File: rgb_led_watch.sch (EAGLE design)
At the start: 30 parts, among them IC4 74V1T126CTR

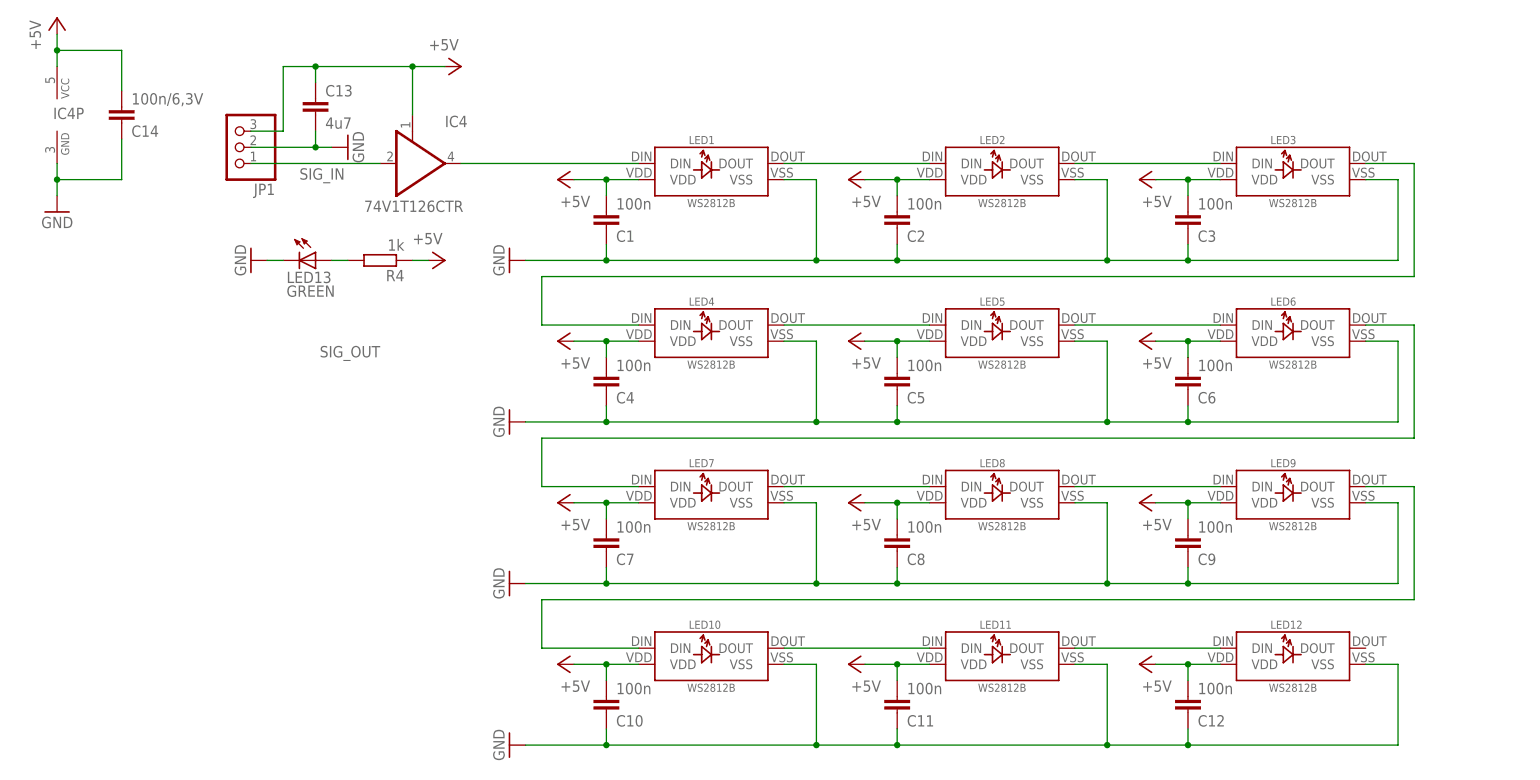
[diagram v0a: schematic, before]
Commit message: v1.2: pridan kapacitni senzor
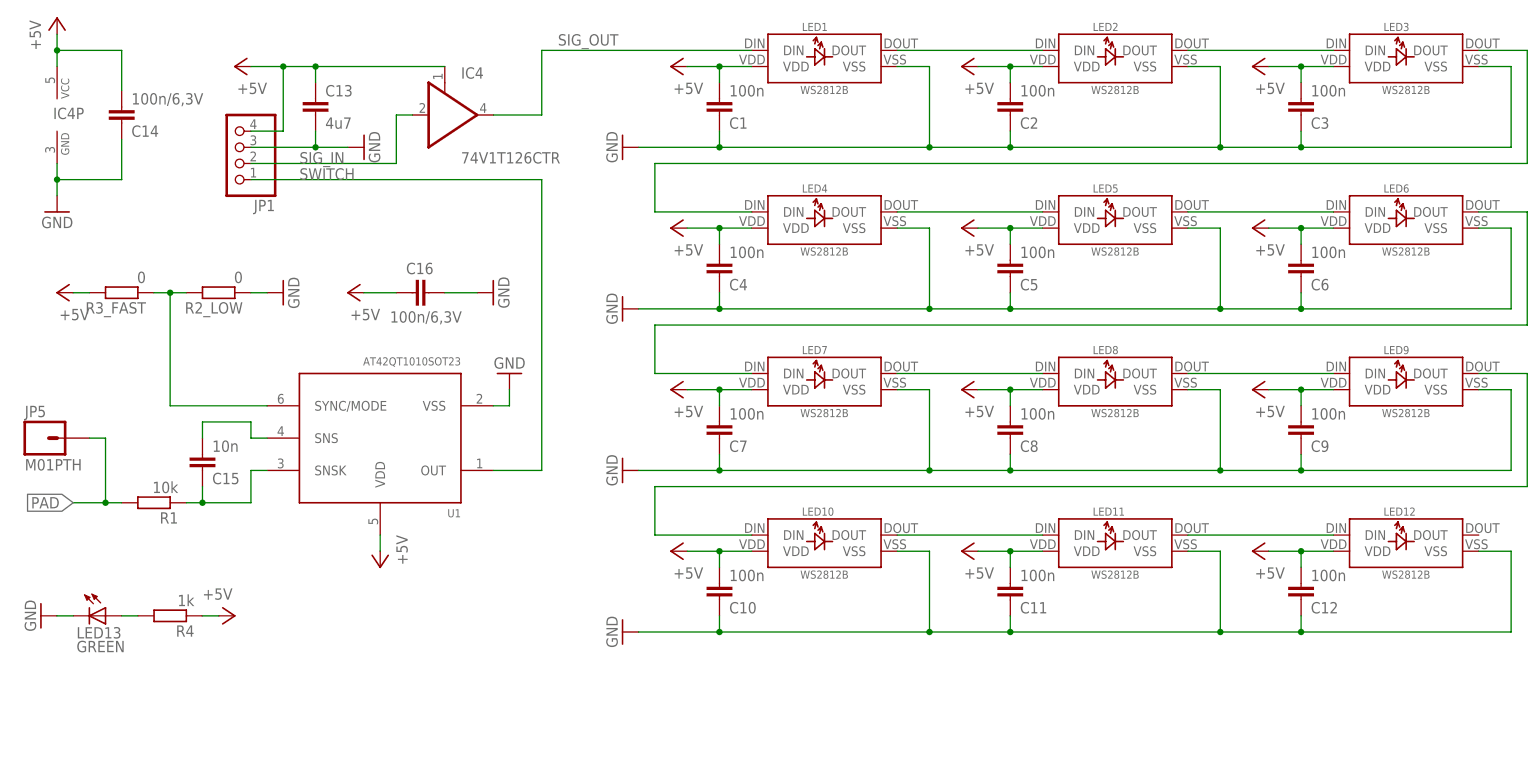
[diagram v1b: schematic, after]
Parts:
- added C15: 10n, rcl_upravena:C-EUC0603
- added C16: 100n/6,3V, rcl_upravena:C-EUC0603
- added JP5: M01PTH, SparkFun-Connectors:M01PTH
- added R1: 10k, rcl:R-EU_R0603
- added R2_LOW, R3_FAST: 0, rcl:R-EU_R0603
- added U1: AT42QT1010SOT23, SparkFun-DigitalIC:AT42QT1010SOT23
- JP1: device pinhead:PINHD-1X3/90 -> pinhead:PINHD-1X4/90
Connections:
- new net PAD: JP5.1, R1.2
- new net SNS: C15.2, U1.SNS
- new net SNSK: C15.1, R1.1, U1.SNSK
- new net SWITCH: JP1.1, U1.OUT
- new net SYNC_MODE: R2_LOW.2, R3_FAST.1, U1.SYNC/MODE
- net +5V: now also C16.1, JP1.4, R3_FAST.2, U1.VDD; no longer JP1.3
- net GND: now also C16.2, JP1.3, R2_LOW.1, U1.VSS; no longer JP1.2
- net SIG_IN: now also JP1.2; no longer JP1.1
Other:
- moved on the sheet: C1, C10, C11, C12, C2, C3, C4, C5, C6, C7, C8, C9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

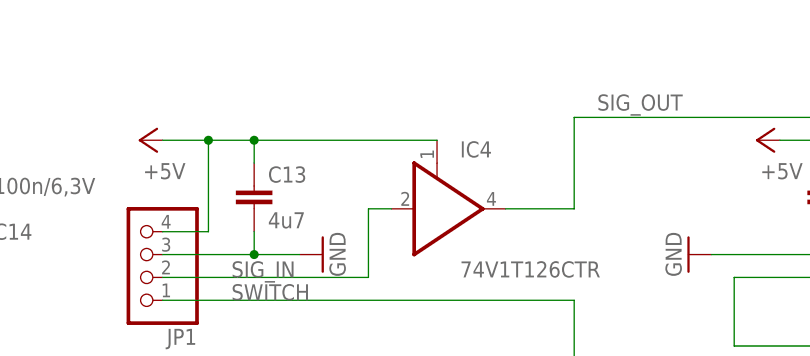
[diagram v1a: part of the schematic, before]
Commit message: v1.3: upraven tvar do podoby hodinek (pridelany ouska) - pripraveno do vyroby
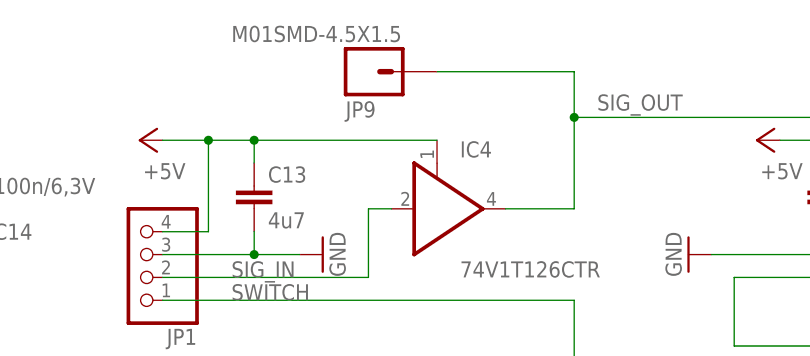
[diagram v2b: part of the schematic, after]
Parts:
- added JP9: M01SMD-4.5X1.5, SparkFun-Connectors:M01SMD-4.5X1.5
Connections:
- net SIG_OUT: now also JP9.1
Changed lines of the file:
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@@
 <part name="R2_LOW" library="rcl" deviceset="R-EU_" device="R0603" value="0"/>
 <part name="R3_FAST" library="rcl" deviceset="R-EU_" device="R0603" value="0"/>
+<part name="JP9" library="SparkFun-Connectors" deviceset="M01" device="SMD-4.5X1.5"/>
 </parts>
 <sheets>
@@
 <instance part="R2_LOW" gate="G$1" x="-58.42" y="-7.62" rot="R180"/>
 <instance part="R3_FAST" gate="G$1" x="-73.66" y="-7.62" rot="R180"/>
+<instance part="JP9" gate="G$1" x="-30.48" y="35.56" smashed="yes" rot="MR180">
+<attribute name="VALUE" x="-45.72" y="40.64" size="1.778" layer="96" rot="MR180"/>
+<attribute name="NAME" x="-33.02" y="32.258" size="1.778" layer="95" rot="MR180"/>
+</instance>
 </instances>
 <busses>
@@
 <label x="-5.08" y="33.02" size="1.778" layer="95" rot="MR180"/>
 <pinref part="LED1" gate="G$1" pin="DIN"/>
-</segment>
-</net>
+<wire x1="-22.86" y1="35.56" x2="-7.62" y2="35.56" width="0.1524" layer="91"/>
+<pinref part="JP9" gate="G$1" pin="1"/>
+<wire x1="-7.62" y1="35.56" x2="-7.62" y2="30.48" width="0.1524" layer="91"/>
+<junction x="-7.62" y="30.48"/>
+</segment>
+</net>

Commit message: hodinky
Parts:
- removed C14, C16: 100n/6,3V, rcl_upravena:C-EUC0603
- removed C15: 10n, rcl_upravena:C-EUC0603
- removed IC4: 74V1T126CTR, 74xx-little-de:74AHC1G126DCK
- removed JP5: M01PTH, SparkFun-Connectors:M01PTH
- removed JP9: M01SMD-4.5X1.5, SparkFun-Connectors:M01SMD-4.5X1.5
- removed R2_LOW, R3_FAST: 0, rcl:R-EU_R0603
- removed U1: AT42QT1010SOT23, SparkFun-DigitalIC:AT42QT1010SOT23
- added C17, C18, C19, C20: 100nF, rcl_upravena:C-EUC0306
- added C21, C22: 10nF, rcl_upravena:C-EUC0805
- added L1: 10uH, rcl_upravena:L-EUSMD0805
- added L2: FB, rcl_upravena:L-EUSMD0603
- added LED14: WS2812B, rgb_led:WS2812B
- added LED15: (no value), led:LED5MM
- added U$2: ATXMEGA128A4U_AU, xmega:ATXMEGA128A4U_AU
- C13: value 4u7 -> 100n; device rcl_upravena:C-EUC0603 -> resistor:C-EUC0603
- JP1: device pinhead:PINHD-1X4/90 -> pinhead:PINHD-1X6/90
- R1: value 10k -> 1k; device rcl:R-EU_R0603 -> rcl_upravena:R-EU_R0603
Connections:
- removed net PAD: JP5.1, R1.2
- removed net SIG_IN: IC4A.I, JP1.2
- removed net SNS: C15.2, U1.SNS
- removed net SNSK: C15.1, R1.1, U1.SNSK
- removed net SWITCH: JP1.1, U1.OUT
- removed net SYNC_MODE: R2_LOW.2, R3_FAST.1, U1.SYNC/MODE
- new net +3V3: JP1.1, L1.1
- new net N$1: C17.2, C18.2, C19.2, C21.2, L1.2, L2.1
- new net N$11: C20.1, C22.1, L2.2, U$2.AVCC
- new net N$13: JP1.6, U$2.PE3
- new net N$14: U$2.RESET
- new net N$15: JP1.3, U$2.PDI_DATA
- new net N$16: LED12.DOUT, LED14.DIN
- new net N$17: JP1.5, U$2.PE2
- new net N$18: LED15.A, R1.2
- new net N$19: R1.1, U$2.PC3
- net +5V: now also C13.2, LED14.VDD; no longer C13.1, C14.2, C16.1, IC4A.OE, IC4P.VCC, JP1.4, R3_FAST.2, U1.VDD
- net GND: now also C13.1, C17.1, C18.1, C19.1, C20.2, C21.1, C22.2, JP1.2, LED14.VSS, LED15.C, U$2.AGND, U$2.GND1, U$2.GND2, U$2.GND3, U$2.VCC1, U$2.VCC2, U$2.VCC3; no longer C13.2, C14.1, C16.2, IC4P.GND, JP1.3, R2_LOW.1, U1.VSS
- net SIG_OUT: now also U$2.PD3; no longer IC4A.O, JP9.1
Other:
- moved on the sheet: C13, R1
